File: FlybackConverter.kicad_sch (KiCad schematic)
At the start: 35 parts, among them J1 USB_C_Receptacle_PowerOnly_6P, T1 Transformer_1P_2S, U1 LNK6428K, U2 TPS25820DSST

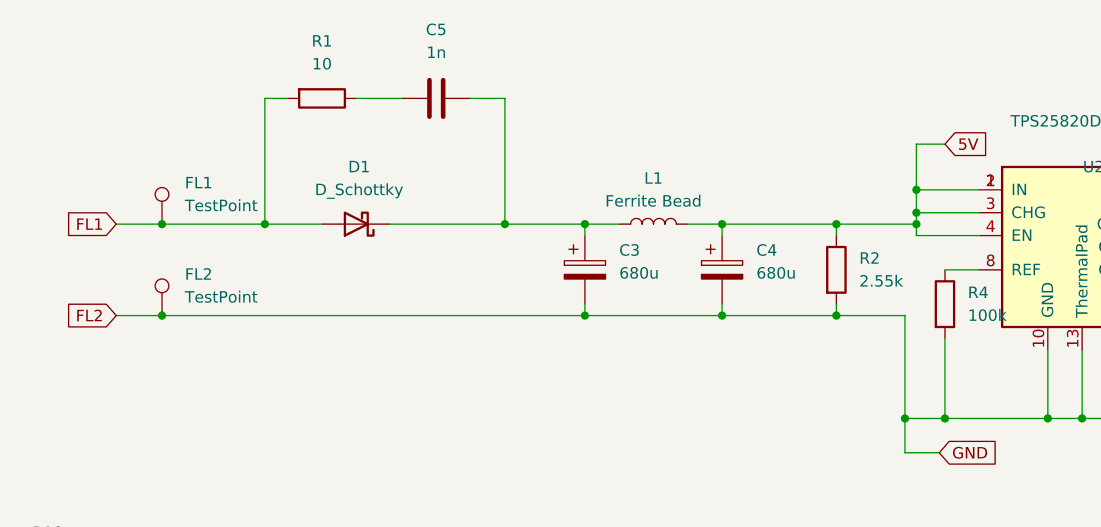
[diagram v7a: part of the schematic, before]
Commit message: パスコン設置 fix #1
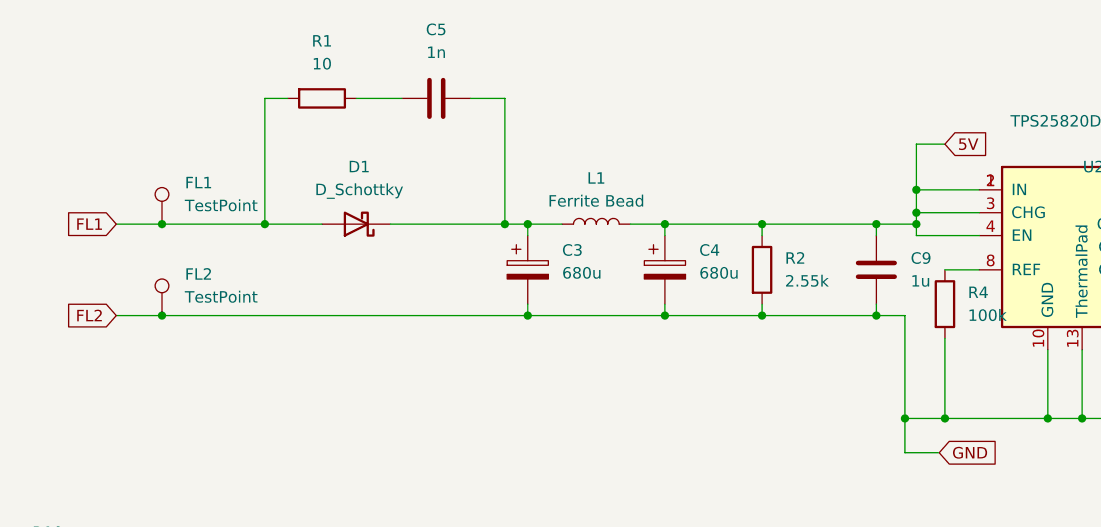
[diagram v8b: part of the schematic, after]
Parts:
- added C9: 1u, Capacitor_SMD:C_0805_2012Metric, symbol Device:C
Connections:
- net 5V: now also C9.1
- net FL2: now also C9.2
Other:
- moved on the sheet: C3, C4, L1, R2
